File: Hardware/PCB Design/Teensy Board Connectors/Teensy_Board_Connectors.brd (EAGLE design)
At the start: 75.7 x 64.3 mm, 12 parts

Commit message: Added ULN2803 with SOP18 PKG for the connector board
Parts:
- added IC1, IC2, IC3: (no value), CBLA_Test_bed_Library:SOP18
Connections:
- new net GND: IC1.9, IC2.9, IC3.9
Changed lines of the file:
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@@
 <attribute name="OC_FARNELL" value="unknown" x="70.612" y="27.686" size="1.778" layer="27" rot="R90" display="off"/>
 </element>
+<element name="IC1" library="CBLA_Test_bed_Library" package="SOP18" value="" x="7.62" y="10.16"/>
+<element name="IC2" library="CBLA_Test_bed_Library" package="SOP18" value="" x="7.62" y="0"/>
+<element name="IC3" library="CBLA_Test_bed_Library" package="SOP18" value="" x="7.62" y="-10.16"/>
 </elements>
 <signals>
@@
 <signal name="SPWM_5_3">
 </signal>
+<signal name="GND">
+<contactref element="IC1" pad="9"/>
+<contactref element="IC2" pad="9"/>
+<contactref element="IC3" pad="9"/>
+<wire x1="12.7" y1="-3.6" x2="12.7" y2="6.56" width="0" layer="19" extent="1-1"/>
+<wire x1="12.7" y1="-13.76" x2="12.7" y2="-3.6" width="0" layer="19" extent="1-1"/>
+</signal>
 </signals>

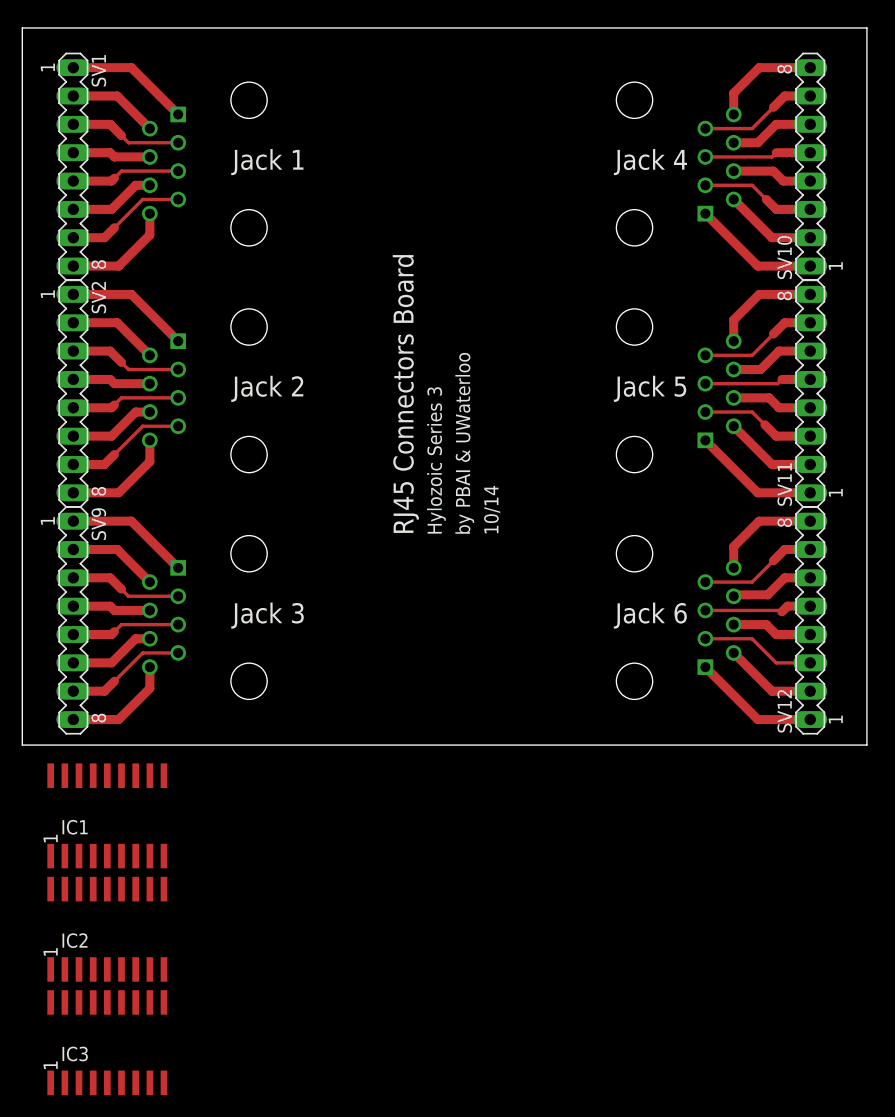
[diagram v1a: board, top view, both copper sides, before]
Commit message: Updated signal LEDS
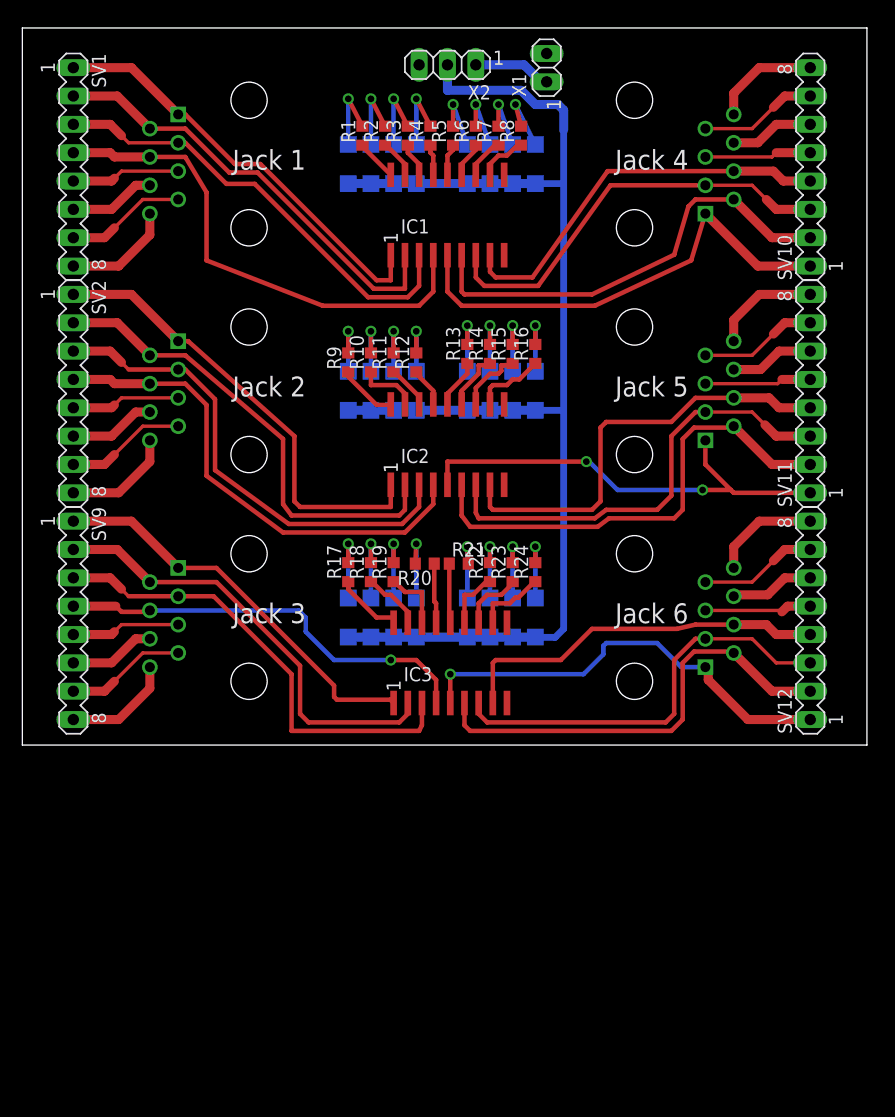
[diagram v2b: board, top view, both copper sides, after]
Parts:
- added LED1, LED10, LED11, LED12, LED13, LED14, LED15, LED16, LED17, LED18, LED19, LED2, LED20, LED21, LED22, LED23, LED24, LED3, LED4, LED5, LED6, LED7, LED8, LED9: (no value), led:SML1206
- added R1, R10, R11, R12, R13, R14, R15, R16, R17, R18, R19, R2, R20, R21, R22, R23, R24, R3, R4, R5, R6, R7, R8, R9: 470, CBLA_Test_bed_Library:R0603
- added X1: (no value), CBLA_Test_bed_Library:1X02
- added X2: (no value), CBLA_Test_bed_Library:1X03
- moved IC1 61.9 mm to (38.1, 64.0)
- moved IC2 53.1 mm to (38.1, 43.4)
- moved IC3 45.9 mm to (38.4, 23.9)
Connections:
- new net +5V: LED1.A, LED10.A, LED11.A, LED12.A, LED13.A, LED14.A, LED15.A, LED16.A, LED17.A, LED18.A, LED19.A, LED2.A, LED20.A, LED21.A, LED22.A, LED23.A, LED24.A, LED3.A, LED4.A, LED5.A, LED6.A, LED7.A, LED8.A, LED9.A, X2.2
- new net +5VJUMP: X1.1, X2.1
- new net N$1: IC1.18, R1.1
- new net N$10: IC1.11, R8.1
- new net N$11: LED2.C, R2.2
- new net N$12: LED3.C, R3.2
- new net N$13: LED4.C, R4.2
- new net N$14: LED5.C, R5.2
- new net N$15: LED6.C, R6.2
- new net N$16: LED7.C, R7.2
- new net N$17: LED8.C, R8.2
- new net N$18: IC2.18, R9.1
- new net N$19: LED9.C, R9.2
- new net N$2: LED1.C, R1.2
- new net N$20: IC2.17, R10.1
- new net N$21: IC2.16, R11.1
- new net N$22: IC2.15, R12.1
- new net N$23: IC2.14, R13.1
- new net N$24: IC2.13, R14.1
- new net N$25: IC2.12, R15.1
- new net N$26: IC2.11, R16.1
- new net N$27: LED10.C, R10.2
- new net N$28: LED11.C, R11.2
- new net N$29: LED12.C, R12.2
- new net N$3: IC1.17, R2.1
- new net N$30: LED13.C, R13.2
- new net N$31: LED14.C, R14.2
- new net N$32: LED15.C, R15.2
- new net N$33: LED16.C, R16.2
- new net N$34: IC3.18, R17.1
- new net N$35: LED17.C, R17.2
- new net N$36: IC3.17, R18.1
- new net N$37: IC3.16, R19.1
- new net N$38: IC3.15, R20.1
- new net N$39: IC3.14, R21.1
- new net N$4: IC1.16, R3.1
- new net N$40: IC3.13, R22.1
- new net N$41: IC3.12, R23.1
- new net N$42: IC3.11, R24.1
- new net N$43: LED18.C, R18.2
- new net N$44: LED19.C, R19.2
- new net N$45: LED20.C, R20.2
- new net N$46: LED21.C, R21.2
- new net N$47: LED22.C, R22.2
- new net N$48: LED23.C, R23.2
- new net N$49: LED24.C, R24.2
- new net N$5: IC1.15, R4.1
- new net N$6: IC1.14, R5.1
- new net N$7: IC1.13, R6.1
- new net N$8: IC1.12, R7.1
- net FPWM_1_1: now also IC1.1
- net FPWM_1_2: now also IC1.2
- net FPWM_2_1: now also IC2.1
- net FPWM_2_2: now also IC2.2
- net FPWM_4_1: now also IC1.5
- net FPWM_4_2: now also IC1.6
- net FPWM_5_1: now also IC2.5
- net FPWM_5_2: now also IC2.6
- net GND: now also X1.2
- net SPWM_1_1: now also IC1.3
- net SPWM_1_2: now also IC1.4
- net SPWM_2_1: now also IC2.3
- net SPWM_2_2: now also IC2.4
- net SPWM_3_1: now also IC3.1
- net SPWM_3_2: now also IC3.2
- net SPWM_3_3: now also IC3.3
- net SPWM_3_4: now also IC3.4
- net SPWM_4_1: now also IC1.7
- net SPWM_4_2: now also IC1.8
- net SPWM_5_1: now also IC2.7
- net SPWM_5_2: now also IC2.8
- net SPWM_6_1: now also IC3.5
- net SPWM_6_2: now also IC3.6
- net SPWM_6_3: now also IC3.7
- net SPWM_6_4: now also IC3.8
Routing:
- net +5V: track 0.00 -> 124.3 mm
- net FPWM_5_2: track 8.28 -> 48.9 mm
- net SPWM_2_2: track 7.02 -> 47.2 mm
- net SPWM_1_2: track 7.02 -> 44.9 mm
- net SPWM_2_1: track 10.1 -> 47.8 mm
- net SPWM_6_2: track 8.28 -> 45.5 mm
- net SPWM_3_3: track 10.1 -> 46.6 mm
- net FPWM_2_2: track 8.07 -> 42.5 mm
- net SPWM_3_2: track 8.07 -> 40.2 mm
- net FPWM_4_2: track 8.28 -> 40.3 mm
- net SPWM_5_2: track 7.23 -> 39.2 mm
- net FPWM_1_2: track 8.07 -> 39.9 mm
- net SPWM_3_4: track 7.02 -> 38.2 mm, vias 0 -> 1
- net FPWM_4_1: track 11.3 -> 42.3 mm
- net SPWM_1_1: track 10.1 -> 40.6 mm
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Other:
- board text added: "ON"

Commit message: Updated Teensy Board and Connector Board design
- fixed broken connection
- makes everything 45 degrees bend
- moved the RJ45 connectors a bit to the right so they don't interfere
with the power header
- connect common pin to _5V
- added power and ground pour
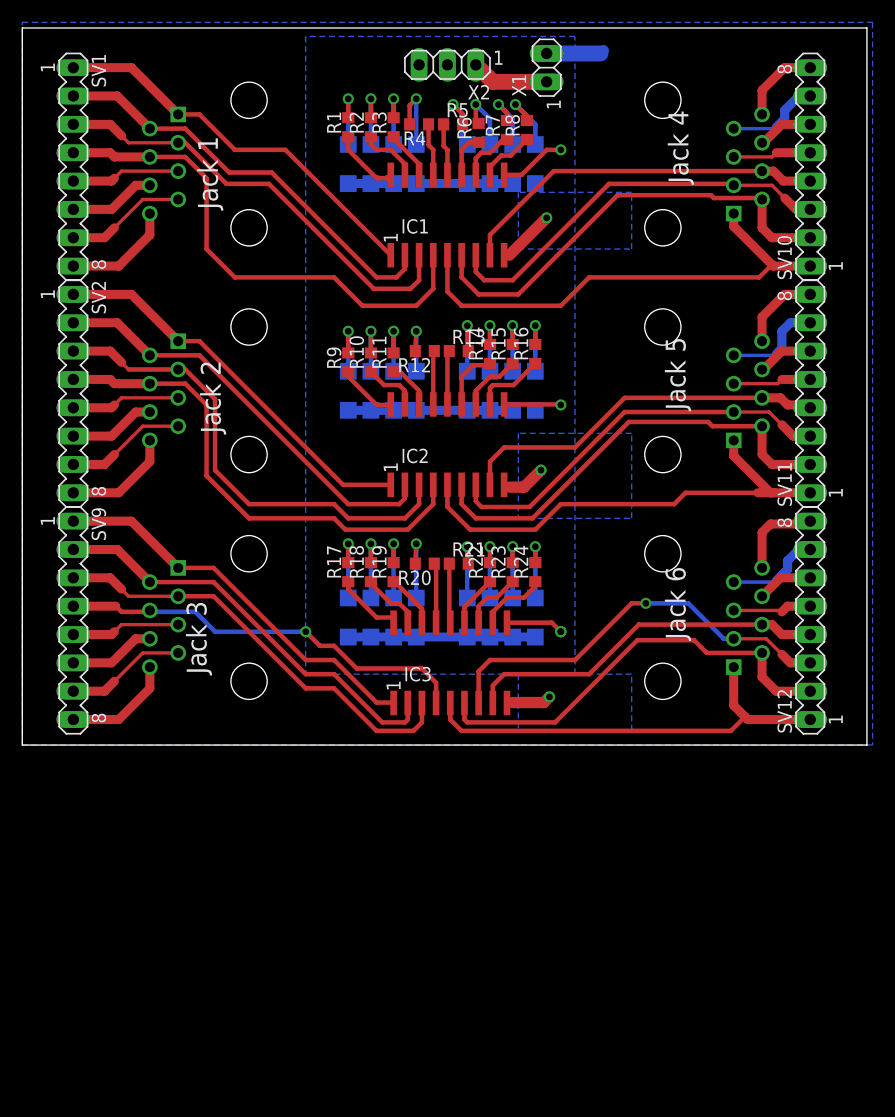
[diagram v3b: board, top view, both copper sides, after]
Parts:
- moved SV6 2.54 mm to (57.4, 68.6)
- moved SV7 2.54 mm to (57.4, 48.3)
- moved SV8 2.54 mm to (57.4, 27.9)
- moved R1 1.48 mm to (29.2, 71.9)
- moved R2 1.48 mm to (31.2, 71.9)
- moved R3 1.48 mm to (33.3, 71.9)
- moved R4 1.44 mm to (35.6, 72.1), turned to 180 degrees
- moved R12 1.27 mm to (36.1, 51.8), turned to 180 degrees
- moved R5 1.02 mm to (38.6, 72.1), turned to 0 degrees
- moved R7 0.92 mm to (43.4, 71.6)
- moved R13 0.80 mm to (39.1, 51.8), turned to 0 degrees
- moved R8 0.72 mm to (45.2, 71.6)
- moved R6 0.36 mm to (40.9, 71.4)
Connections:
- net +5V: now also IC1.10, IC2.10, IC3.10
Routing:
- net +5V: track 124.3 -> 62.5 mm, vias 0 -> 4
- net GND: track 0.00 -> 19.5 mm, vias 0 -> 3
- net FPWM_5_2: track 48.9 -> 40.1 mm
- net SPWM_3_3: track 46.6 -> 39.0 mm
- net SPWM_6_2: track 45.5 -> 38.8 mm
- net FPWM_2_1: track 41.5 -> 35.5 mm
- net SPWM_5_2: track 39.2 -> 33.5 mm
- net FPWM_2_2: track 42.5 -> 37.9 mm
- net SPWM_5_1: track 40.7 -> 36.1 mm
- net FPWM_1_1: track 38.6 -> 35.4 mm
- net FPWM_5_1: track 41.1 -> 44.2 mm, vias 2 -> 0
- net A1: track 7.54 -> 5.00 mm
- net A9: track 7.54 -> 5.00 mm
- net A3: track 7.54 -> 5.00 mm
- net A2: track 9.56 -> 7.02 mm
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- added copper zone on layer 16, net +5V
- added copper zone on layer 16, net GND
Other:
- board text added: "12/14"
- board text added: "FPWM1_1"
- board text added: "FPWM1_2"
- board text added: "FPWM2_1"
- board text added: "FPWM2_2"
- board text added: "FPWM4_1"
- board text added: "FPWM4_2"
- board text added: "FPWM5_1"
- board text added: "FPWM5_2"
- board text added: "SPWM1_1"
- board text added: "SPWM1_2"
- board text added: "SPWM2_1"
- board text added: "SPWM2_2"
- board text added: "SPWM3_1"
- board text added: "SPWM3_2"
- board text added: "SPWM3_3"
- board text added: "SPWM3_4"
- board text added: "SPWM4_1"
- board text added: "SPWM4_2"
- board text added: "SPWM5_1"
- board text added: "SPWM5_2"
- board text added: "SPWM6_1"
- board text added: "SPWM6_2"
- board text added: "SPWM6_3"
- board text added: "SPWM6_4"
- board text removed: "10/14"
